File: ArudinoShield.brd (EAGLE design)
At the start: 54.6 x 67 mm, 25 parts, among them IC1 L298

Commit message: minor board changes
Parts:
- moved D5 5.68 mm to (58.4, 38.1), turned to 0 degrees
- moved D1 5.08 mm to (48.3, 34.3)
- moved C2 3.81 mm to (68.6, 41.9)
- moved D4 3.81 mm to (44.5, 50.8)
- moved OUT3 2.54 mm to (71.1, 72.4)
- moved OUT4 2.54 mm to (61.0, 72.4)
- moved D3 2.54 mm to (72.4, 62.2)
- moved D7 2.54 mm to (72.4, 58.4)
- moved D2 1.27 mm to (69.8, 31.8)
- moved D6 1.27 mm to (69.8, 27.9)
- moved C1 1.27 mm to (45.7, 29.2)
- moved D8 1.27 mm to (53.3, 63.5)
- renumbered VREG to U1
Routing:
- net OUT3: track 36.9 -> 19.8 mm
- net VIN: track 148.6 -> 137.6 mm
- net +5VIN: track 58.9 -> 53.0 mm
- net +5V: track 114.1 -> 109.8 mm
- net GND: track 14.7 -> 10.5 mm
- net OUT1: track 27.3 -> 25.2 mm
- net OUT2: track 26.9 -> 28.3 mm
- net OUT4: track 28.0 -> 29.2 mm
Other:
- board size 54.6 x 67 mm -> 54.6 x 64.4 mm

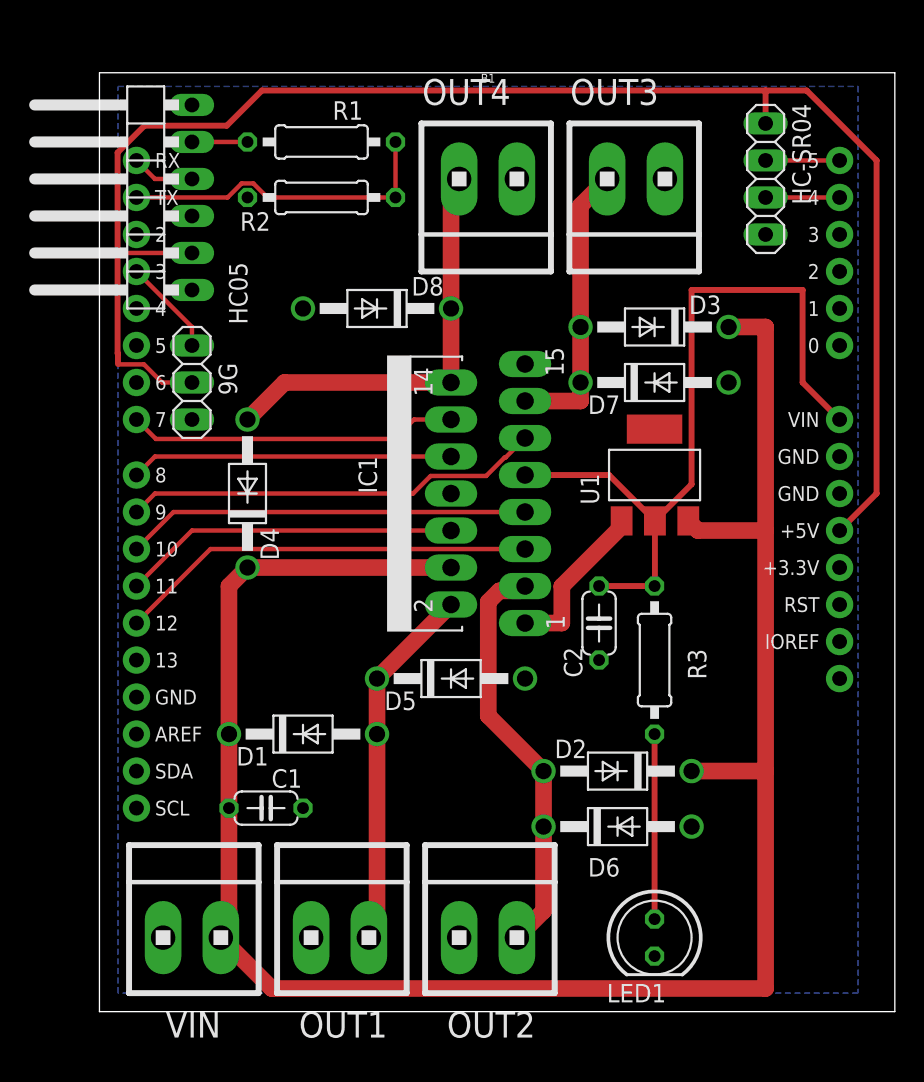
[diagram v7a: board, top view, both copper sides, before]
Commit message: reworked to fit on top of arduino
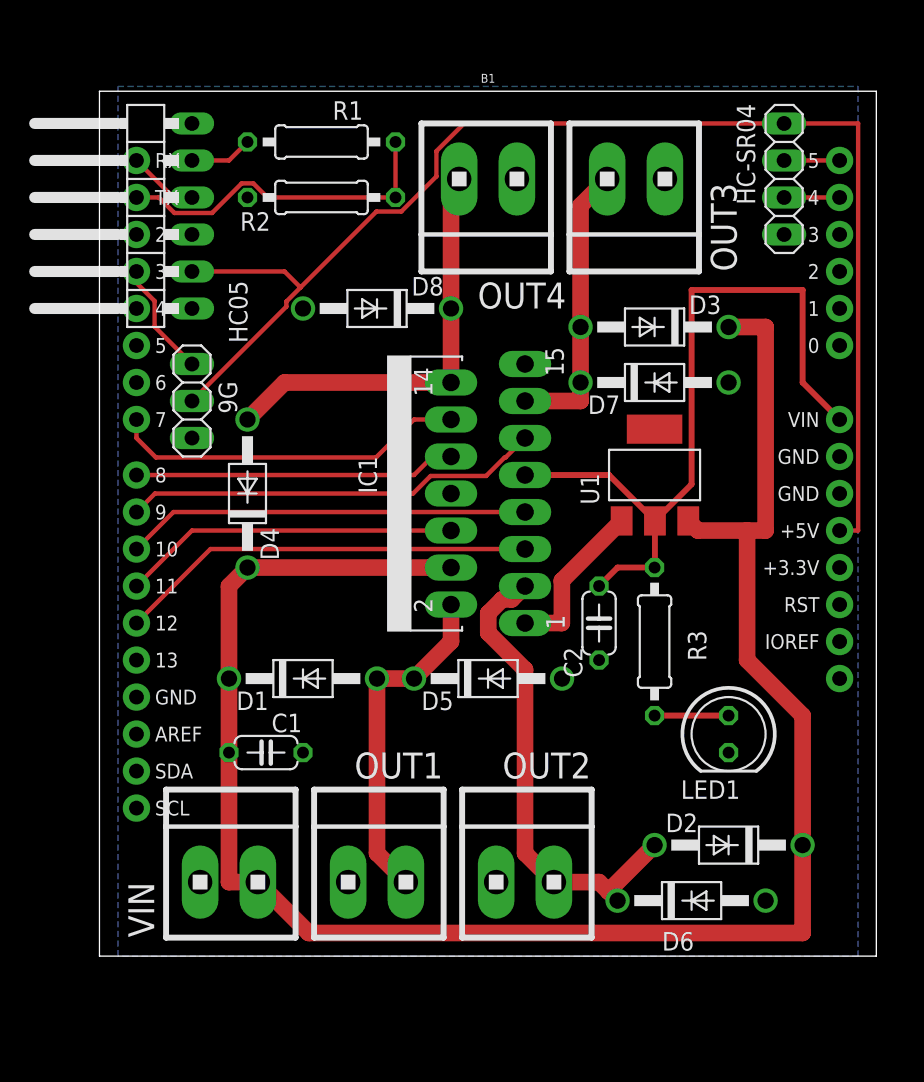
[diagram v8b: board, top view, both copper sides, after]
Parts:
- moved LED1 14.9 mm to (77.5, 34.3)
- moved D2 9.16 mm to (77.5, 26.7)
- moved D6 7.18 mm to (74.9, 22.9)
- moved OUT1 4.58 mm to (53.3, 24.1)
- moved OUT2 4.58 mm to (63.5, 24.1)
- moved VIN 4.58 mm to (43.2, 24.1)
- moved C1 3.81 mm to (45.7, 33.0)
- moved D1 3.81 mm to (48.3, 38.1)
- moved D5 2.54 mm to (61.0, 38.1)
- moved HC05 1.27 mm to (36.8, 69.8)
- moved 9G 1.27 mm to (40.6, 57.1)
- moved R3 1.27 mm to (72.4, 40.6)
- moved HC-SR04 1.27 mm to (81.3, 72.4)
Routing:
- net +5V: track 109.8 -> 91.9 mm
- net VIN: track 137.6 -> 128.2 mm
- net N$25: track 12.7 -> 5.08 mm
- net OUT2: track 28.3 -> 33.0 mm
- net IN4: track 22.7 -> 24.5 mm
- net OUT1: track 25.2 -> 23.5 mm
- net 9GPWM: track 6.66 -> 7.93 mm
- net TRIG: track 5.08 -> 3.81 mm
- net ECHO: track 5.08 -> 3.81 mm
- net N$11: track 22.4 -> 23.3 mm
- net GND: track 10.5 -> 11.2 mm
- net +5VIN: track 53.0 -> 52.2 mm
- net N$14: track 3.81 -> 4.34 mm
- net N$12: track 4.34 -> 4.86 mm
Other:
- board size 54.6 x 64.4 mm -> 53.3 x 59.4 mm
